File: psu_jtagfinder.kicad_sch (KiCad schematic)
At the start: 14 parts, among them U3 MIC2025-2YM, U5 TLV74033, U7 AD8655

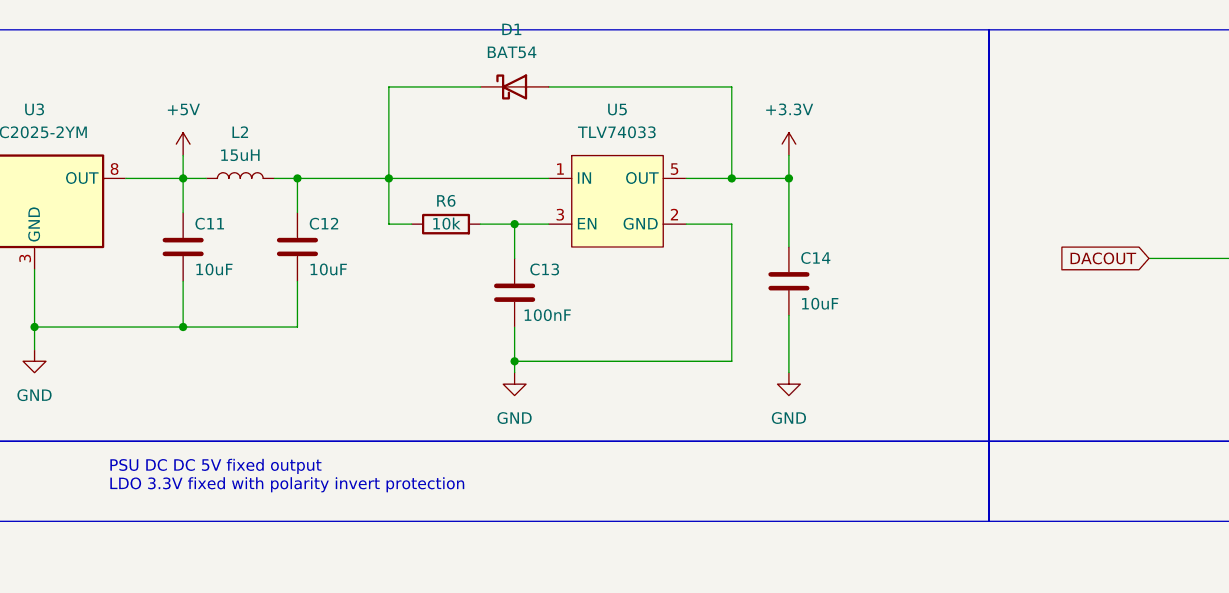
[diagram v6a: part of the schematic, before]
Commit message: update psu CI due thermal problems
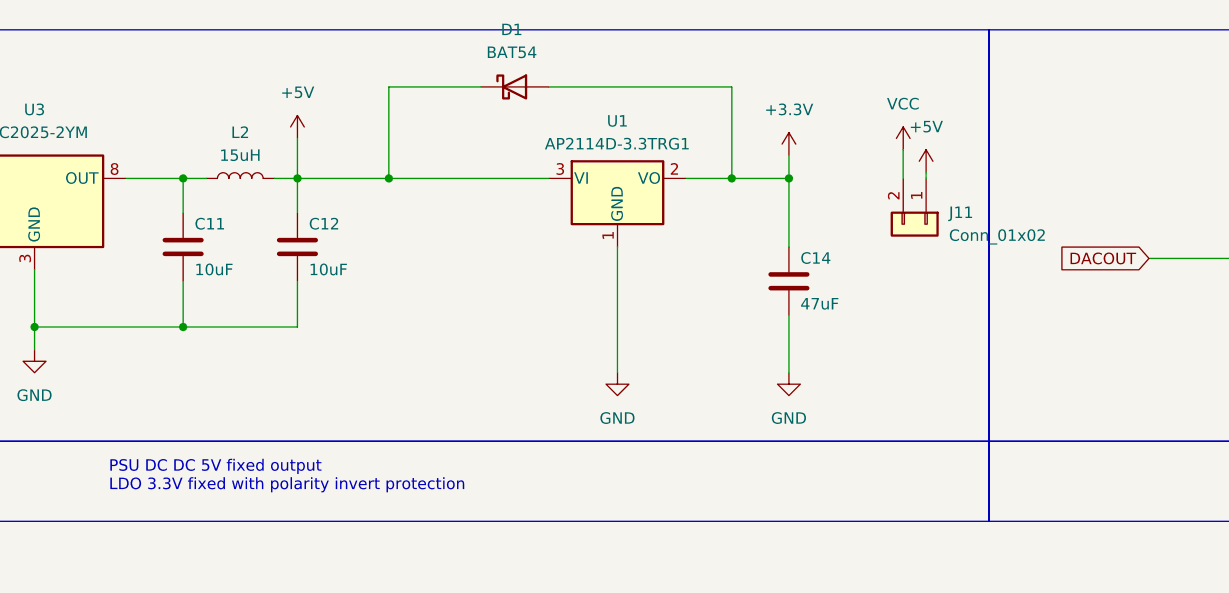
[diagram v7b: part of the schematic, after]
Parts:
- removed C13: 100nF, Capacitor_SMD:C_1206_3216Metric, symbol Device:C
- removed R6: 10k, Resistor_SMD:R_1206_3216Metric, symbol Device:R
- removed U5: TLV74033, Package_TO_SOT_SMD:SOT-23-5, symbol LDO:TLV74033PDBVR
- added J11: Conn_01x02, Connector_PinHeader_2.54mm:PinHeader_1x02_P2.54mm_Vertical, symbol Connector_Generic:Conn_01x02
- added U1: AP2114D-3.3TRG1, Package_TO_SOT_SMD:TO-252-2, symbol Regulator_Linear:AP2127N-3.3
- C14: value 10uF -> 47uF; Fab: KNSCHA -> Panasonic; Man #: RST10UF25V014 -> EEEHA0J470WR
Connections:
- net +3.3V: now also U1.2 (VO)
- net +5V: now also C12.1, D1.1 (K), L2.2, J11.1 (Pin_1), U1.3 (VI); no longer C11.1, L2.1, U3.6 (OUT), U3.8 (OUT)
- net GND: now also U1.1 (GND)
- net VCC: now also J11.2 (Pin_2)
- new net: C11.1, L2.1, U3.6 (OUT), U3.8 (OUT)
